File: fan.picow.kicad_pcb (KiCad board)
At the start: 2 copper layers, 96.5 x 78.2 mm, 61 parts, among them J1 12v Input, J12 Temp, J2 Fan1, J3 Fan2, J4 Fan4, J5 Fan3, J7 OLED, Q1 BSS138, Q2 BSS138, Q3 IRLML9301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

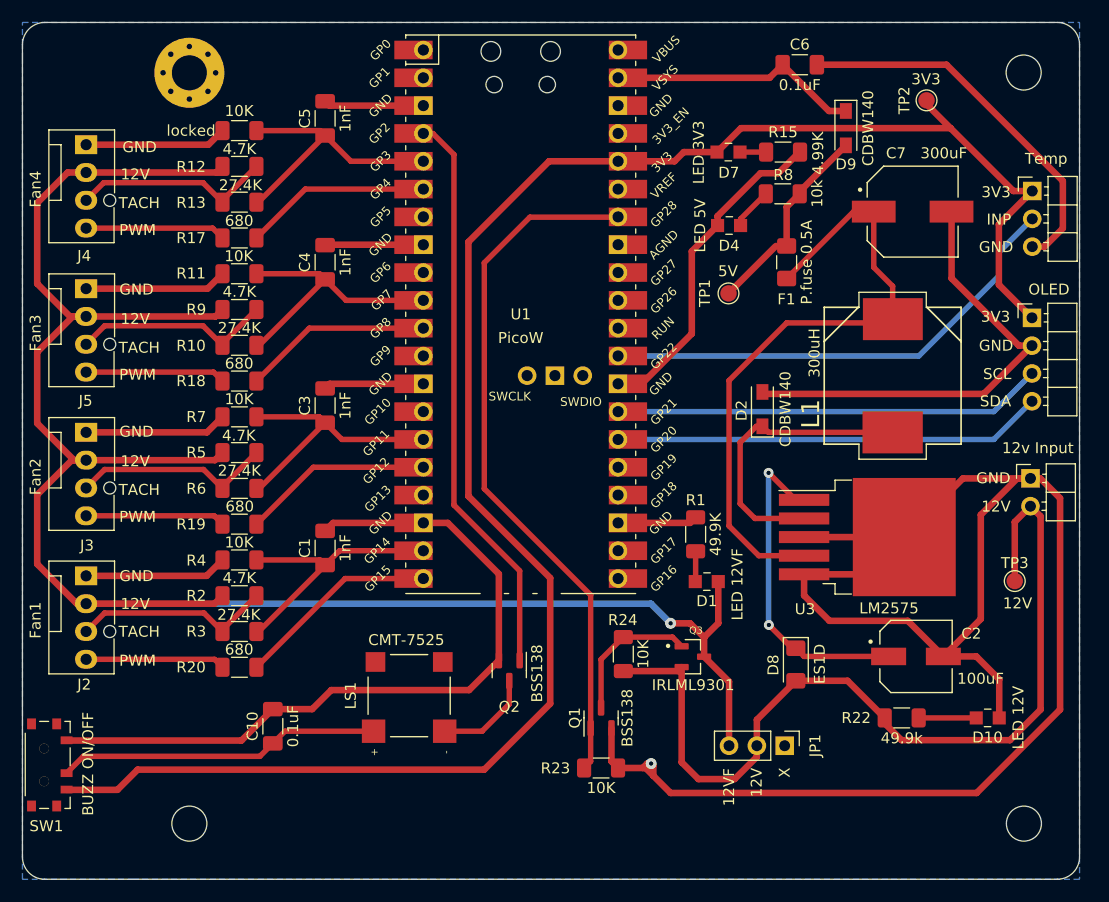
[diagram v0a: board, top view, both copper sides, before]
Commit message: round zone at the corners
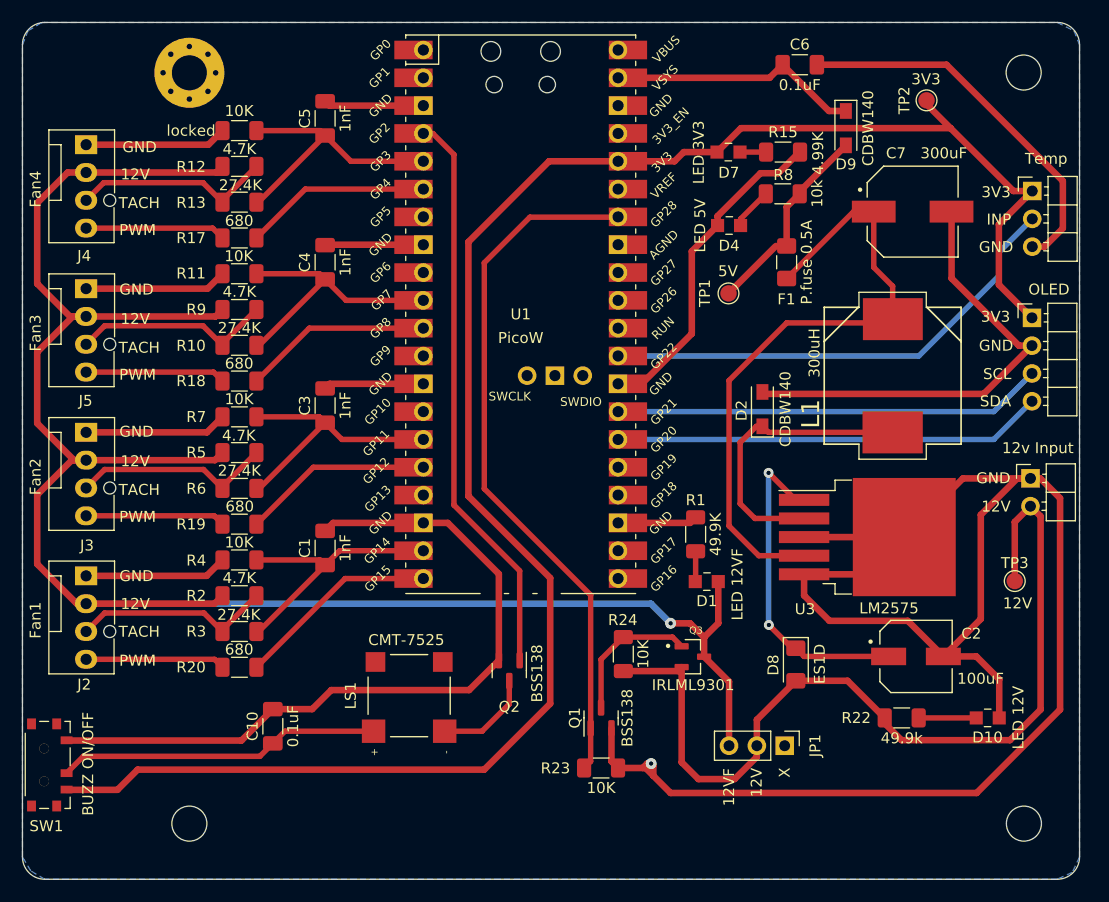
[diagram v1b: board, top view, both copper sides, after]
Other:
- board text added: "0.2000 mm / 0.0000 mm"
- board text added: "0.3000 mm"
- board text added: "1.6000 mm"
- board text added: "2"
- board text added: "96.5200 mm x 78.2320 mm"
- board text added: "BOARD CHARACTERISTICS"
- board text added: "Board Thickness:"
- board text added: "Board overall dimensions:"
- board text added: "Castellated pads:"
- board text added: "Copper Finish:"
- board text added: "Copper Layer Count:"
- board text added: "Edge card connectors:"
- board text added: "Impedance Control:"
- board text added: "Min hole diameter:"
- board text added: "Min track/spacing:"
- board text added: "No"
- board text added: "None"
- board text added: "Plated Board Edge:"

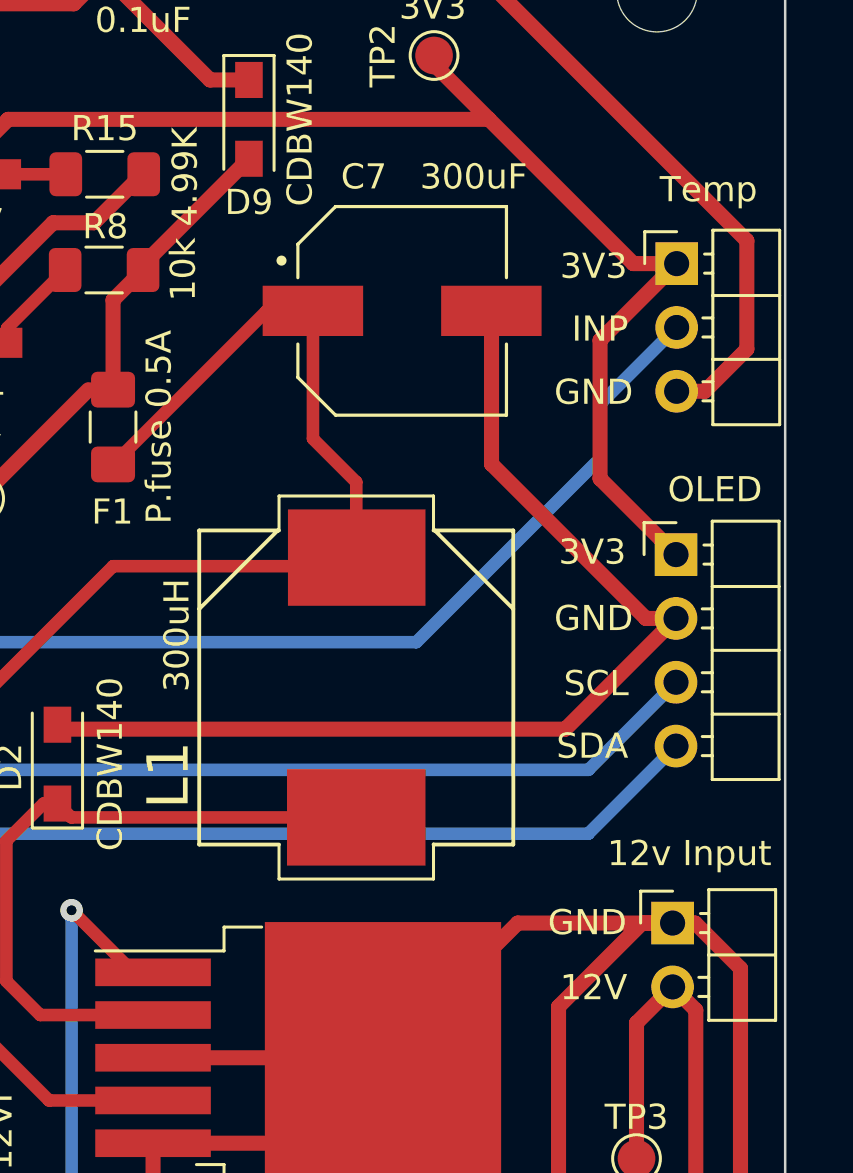
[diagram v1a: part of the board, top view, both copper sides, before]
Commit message: minor changes
- Change L/C values 300 -> 330
- Change footprint association: 12v pinheader is now vertical
- Change 3D models for capacitors (replaced due to lack of stock)
- Also changed some references to make it more neat
- Add also a square around the fan switch area in the schematic
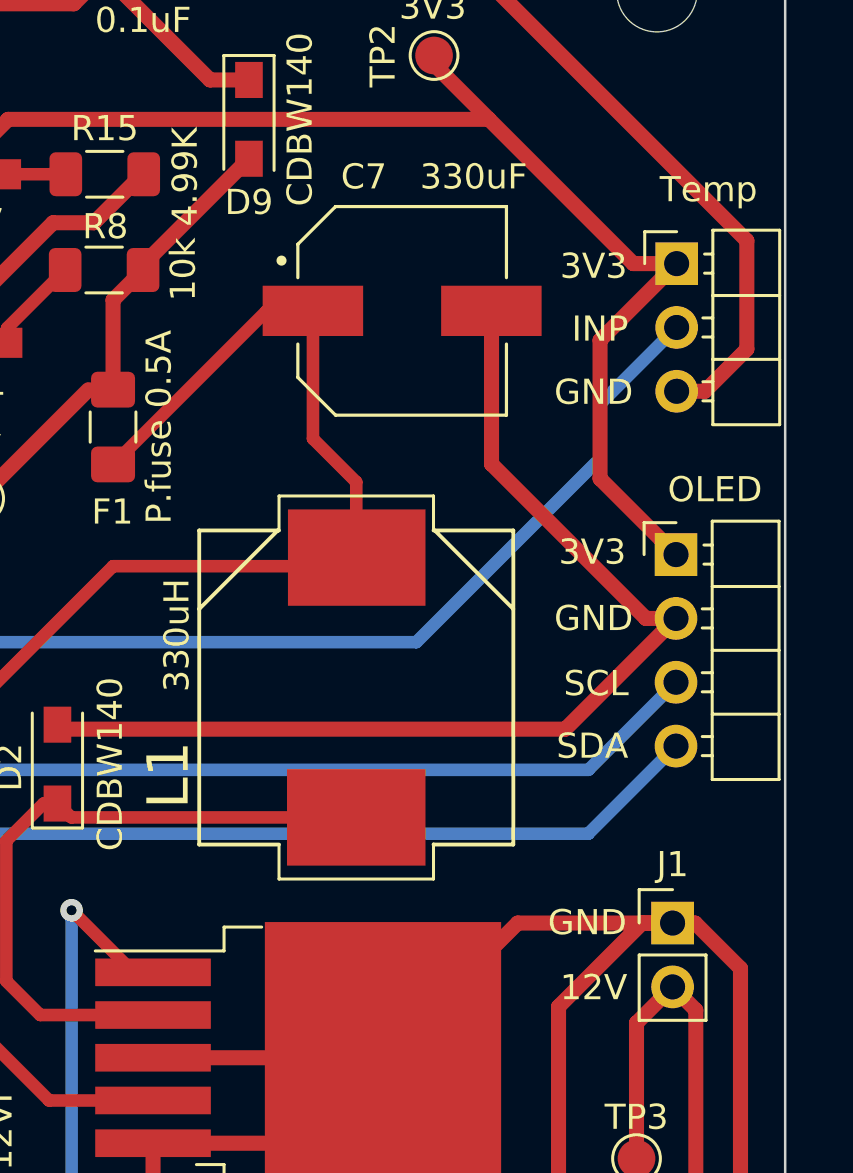
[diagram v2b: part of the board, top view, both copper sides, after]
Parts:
- C7: value 300uF -> 330uF
- J1: footprint Connector_PinHeader_2.54mm:PinHeader_1x02_P2.54mm_Horizontal -> Connector_PinHeader_2.54mm:PinHeader_1x02_P2.54mm_Vertical
- L1: value 300uH -> 330uH
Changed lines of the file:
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@@
     (pad "2" smd rect locked (at 2.5 0) (size 3.2 1.6) (layers "F.Cu" "F.Paste" "F.Mask")
       (net 4 "GND") (pintype "passive"))
-    (model "D:/Users/myria/Documents/KiCad/6.0/3dmodels/EEEHA1V101XP.STEP"
-      (offset (xyz 0 0 0))
-      (scale (xyz 1 1 1))
-      (rotate (xyz -90 0 0))
+    (model "D:/Users/myria/Documents/KiCad/6.0/3dmodels/EXV-9H_KEM.step"
+      (offset (xyz 0 0 0))
+      (scale (xyz 1 1 1))
+      (rotate (xyz 0 0 0))
     )
   )
@@
     )
   )
-  (footprint "Connector_PinHeader_2.54mm:PinHeader_1x02_P2.54mm_Horizontal" (layer "F.Cu")
+  (footprint "Connector_PinHeader_2.54mm:PinHeader_1x02_P2.54mm_Vertical" (layer "F.Cu")
     (at 186.02 82.7786)
-    (descr "Through hole angled pin header, 1x02, 2.54mm pitch, 6mm pin length, single row")
-    (tags "Through hole angled pin header THT 1x02 2.54mm single row")
+    (descr "Through hole straight pin header, 1x02, 2.54mm pitch, single row")
+    (tags "Through hole pin header THT 1x02 2.54mm single row")
     (property "Sheetfile" "File: conectores.kicad_sch")
     (property "Sheetname" "conectores")
     (attr through_hole)
-    (fp_text reference "J1" (at 0.162 5.3594) (layer "F.SilkS") hide
-      (effects (font (size 1 1) (thickness 0.15)))
-    )
-    (fp_text value "12v Input" (at 0.67 -2.7686) (layer "F.SilkS")
-      (effects (font (size 1 1) (thickness 0.15)))
-    )
-    (fp_text user "${REFERENCE}" (at 2.77 1.27 90) (layer "F.Fab")
-      (effects (font (size 1 1) (thickness 0.15)))
-    )
-    (fp_line (start 1.44 1.27) (end 4.1 1.27) (layer "F.SilkS") (width 0.12))
-    (fp_line (start 1.44 3.87) (end 4.1 3.87) (layer "F.SilkS") (width 0.12))
-    (fp_line (start -1.27 -1.27) (end 0 -1.27) (layer "F.SilkS") (width 0.12))
-    (fp_line (start 1.042929 2.92) (end 1.44 2.92) (layer "F.SilkS") (width 0.12))
-    (fp_line (start -1.27 0) (end -1.27 -1.27) (layer "F.SilkS") (width 0.12))
-    (fp_line (start 1.44 -1.33) (end 1.44 3.87) (layer "F.SilkS") (width 0.12))
-    (fp_line (start 1.042929 2.16) (end 1.44 2.16) (layer "F.SilkS") (width 0.12))
-    (fp_line (start 1.11 0.38) (end 1.44 0.38) (layer "F.SilkS") (width 0.12))
-    (fp_line (start 4.1 3.87) (end 4.1 -1.33) (layer "F.SilkS") (width 0.12))
-    (fp_line (start 4.1 -1.33) (end 1.44 -1.33) (layer "F.SilkS") (width 0.12))
-    (fp_line (start 1.11 -0.38) (end 1.44 -0.38) (layer "F.SilkS") (width 0.12))
-    (fp_line (start -1.8 4.35) (end 10.55 4.35) (layer "F.CrtYd") (width 0.05))
-    (fp_line (start 10.55 -1.8) (end -1.8 -1.8) (layer "F.CrtYd") (width 0.05))
-    (fp_line (start 10.55 4.35) (end 10.55 -1.8) (layer "F.CrtYd") (width 0.05))
+    (fp_text reference "J1" (at 0 -2.33) (layer "F.SilkS")
+      (effects (font (size 1 1) (thickness 0.15)))
+    )
+    (fp_text value "12v Input" (at 0 4.87) (layer "F.Fab")
+      (effects (font (size 1 1) (thickness 0.15)))
+    )
+    (fp_text user "${REFERENCE}" (at 0 1.27 90) (layer "F.Fab")
+      (effects (font (size 1 1) (thickness 0.15)))
+    )
+    (fp_line (start -1.33 1.27) (end -1.33 3.87) (layer "F.SilkS") (width 0.12))
+    (fp_line (start -1.33 -1.33) (end 0 -1.33) (layer "F.SilkS") (width 0.12))
+    (fp_line (start -1.33 1.27) (end 1.33 1.27) (layer "F.SilkS") (width 0.12))
+    (fp_line (start -1.33 0) (end -1.33 -1.33) (layer "F.SilkS") (width 0.12))
+    (fp_line (start -1.33 3.87) (end 1.33 3.87) (layer "F.SilkS") (width 0.12))
+    (fp_line (start 1.33 1.27) (end 1.33 3.87) (layer "F.SilkS") (width 0.12))
+    (fp_line (start 1.8 4.35) (end 1.8 -1.8) (layer "F.CrtYd") (width 0.05))
+    (fp_line (start 1.8 -1.8) (end -1.8 -1.8) (layer "F.CrtYd") (width 0.05))
+    (fp_line (start -1.8 4.35) (end 1.8 4.35) (layer "F.CrtYd") (width 0.05))
     (fp_line (start -1.8 -1.8) (end -1.8 4.35) (layer "F.CrtYd") (width 0.05))
-    (fp_line (start 10.04 2.22) (end 10.04 2.86) (layer "F.Fab") (width 0.1))
-    (fp_line (start 4.1 0.04) (end 10.1 0.04) (layer "F.Fab") (width 0.12))
-    (fp_line (start 10.1 2.92) (end 4.1 2.92) (layer "F.Fab") (width 0.12))
-    (fp_line (start 10.1 -0.38) (end 10.1 0.38) (layer "F.Fab") (width 0.12))
-    (fp_line (start -0.32 2.86) (end 1.5 2.86) (layer "F.Fab") (width 0.1))
-    (fp_line (start 4.1 -0.32) (end 10.1 -0.32) (layer "F.Fab") (width 0.12))
-    (fp_line (start 4.1 2.16) (end 10.1 2.16) (layer "F.Fab") (width 0.12))
-    (fp_line (start 10.1 0.38) (end 4.1 0.38) (layer "F.Fab") (width 0.12))
-    (fp_line (start 10.1 2.16) (end 10.1 2.92) (layer "F.Fab") (width 0.12))
-    (fp_line (start 4.04 2.86) (end 10.04 2.86) (layer "F.Fab") (width 0.1))
-    (fp_line (start 4.04 -1.27) (end 4.04 3.81) (layer "F.Fab") (width 0.1))
-    (fp_line (start -0.32 -0.32) (end -0.32 0.32) (layer "F.Fab") (width 0.1))
-    (fp_line (start 1.5 3.81) (end 1.5 -0.635) (layer "F.Fab") (width 0.1))
-    (fp_line (start 4.04 3.81) (end 1.5 3.81) (layer "F.Fab") (width 0.1))
-    (fp_line (start 4.1 0.28) (end 10.1 0.28) (layer "F.Fab") (width 0.12))
-    (fp_line (start 2.135 -1.27) (end 4.04 -1.27) (layer "F.Fab") (width 0.1))
-    (fp_line (start 4.1 -0.38) (end 10.1 -0.38) (layer "F.Fab") (width 0.12))
-    (fp_line (start 4.1 0.16) (end 10.1 0.16) (layer "F.Fab") (width 0.12))
-    (fp_line (start -0.32 0.32) (end 1.5 0.32) (layer "F.Fab") (width 0.1))
-    (fp_line (start 4.04 -0.32) (end 10.04 -0.32) (layer "F.Fab") (width 0.1))
-    (fp_line (start 1.5 -0.635) (end 2.135 -1.27) (layer "F.Fab") (width 0.1))
-    (fp_line (start -0.32 2.22) (end 1.5 2.22) (layer "F.Fab") (width 0.1))
-    (fp_line (start -0.32 2.22) (end -0.32 2.86) (layer "F.Fab") (width 0.1))
-    (fp_line (start 4.1 -0.08) (end 10.1 -0.08) (layer "F.Fab") (width 0.12))
-    (fp_line (start 4.04 2.22) (end 10.04 2.22) (layer "F.Fab") (width 0.1))
-    (fp_line (start 4.04 0.32) (end 10.04 0.32) (layer "F.Fab") (width 0.1))
-    (fp_line (start 4.1 -0.2) (end 10.1 -0.2) (layer "F.Fab") (width 0.12))
-    (fp_line (start -0.32 -0.32) (end 1.5 -0.32) (layer "F.Fab") (width 0.1))
-    (fp_line (start 10.04 -0.32) (end 10.04 0.32) (layer "F.Fab") (width 0.1))
+    (fp_line (start 1.27 3.81) (end -1.27 3.81) (layer "F.Fab") (width 0.1))
+    (fp_line (start -0.635 -1.27) (end 1.27 -1.27) (layer "F.Fab") (width 0.1))
+    (fp_line (start -1.27 -0.635) (end -0.635 -1.27) (layer "F.Fab") (width 0.1))
+    (fp_line (start -1.27 3.81) (end -1.27 -0.635) (layer "F.Fab") (width 0.1))
+    (fp_line (start 1.27 -1.27) (end 1.27 3.81) (layer "F.Fab") (width 0.1))
     (pad "1" thru_hole rect (at 0 0) (size 1.7 1.7) (drill 1) (layers *.Cu *.Mask)
       (net 4 "GND") (pinfunction "Pin_1") (pintype "passive"))
     (pad "2" thru_hole oval (at 0 2.54) (size 1.7 1.7) (drill 1) (layers *.Cu *.Mask)
       (net 5 "/12V") (pinfunction "Pin_2") (pintype "passive"))
-    (model "${KICAD6_3DMODEL_DIR}/Connector_PinHeader_2.54mm.3dshapes/PinHeader_1x02_P2.54mm_Horizontal.wrl"
+    (model "${KICAD6_3DMODEL_DIR}/Connector_PinHeader_2.54mm.3dshapes/PinHeader_1x02_P2.54mm_Vertical.wrl"
       (offset (xyz 0 0 0))
       (scale (xyz 1 1 1))
@@
       (effects (font (size 1.645646 1.645646) (thickness 0.15)))
     )
-    (fp_text value "300uH" (at -2.0828 7.1406 90) (layer "F.SilkS")
+    (fp_text value "330uH" (at -2.0828 7.1406 90) (layer "F.SilkS")
       (effects (font (size 1 1) (thickness 0.15)))
     )
@@
       (effects (font (size 1 1) (thickness 0.15)))
     )
-    (fp_text value "300uF" (at 2.8448 -5.334) (layer "F.SilkS")
+    (fp_text value "330uF" (at 2.8448 -5.334) (layer "F.SilkS")
       (effects (font (size 1 1) (thickness 0.15)))
     )
@@
     (pad "2" smd rect locked (at 3.55 0) (size 4 2) (layers "F.Cu" "F.Paste" "F.Mask")
       (net 4 "GND") (pintype "passive"))
-    (model "D:/Users/myria/Documents/KiCad/6.0/3dmodels/EEEFT1V331AP.step"
-      (offset (xyz 0 0 0))
-      (scale (xyz 1 1 1))
-      (rotate (xyz -90 0 0))
-    )
-  )
+    (model "D:/Users/myria/Documents/KiCad/6.0/3dmodels/CAP_J-V_8X10P5_RUB.step"
+      (offset (xyz 0 0 0))
+      (scale (xyz 1 1 1))
+      (rotate (xyz 0 0 0))
+    )
+  )
